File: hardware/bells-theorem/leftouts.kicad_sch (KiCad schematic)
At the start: 45 parts, among them U10 TL074, U8 TL074, U9 TL074

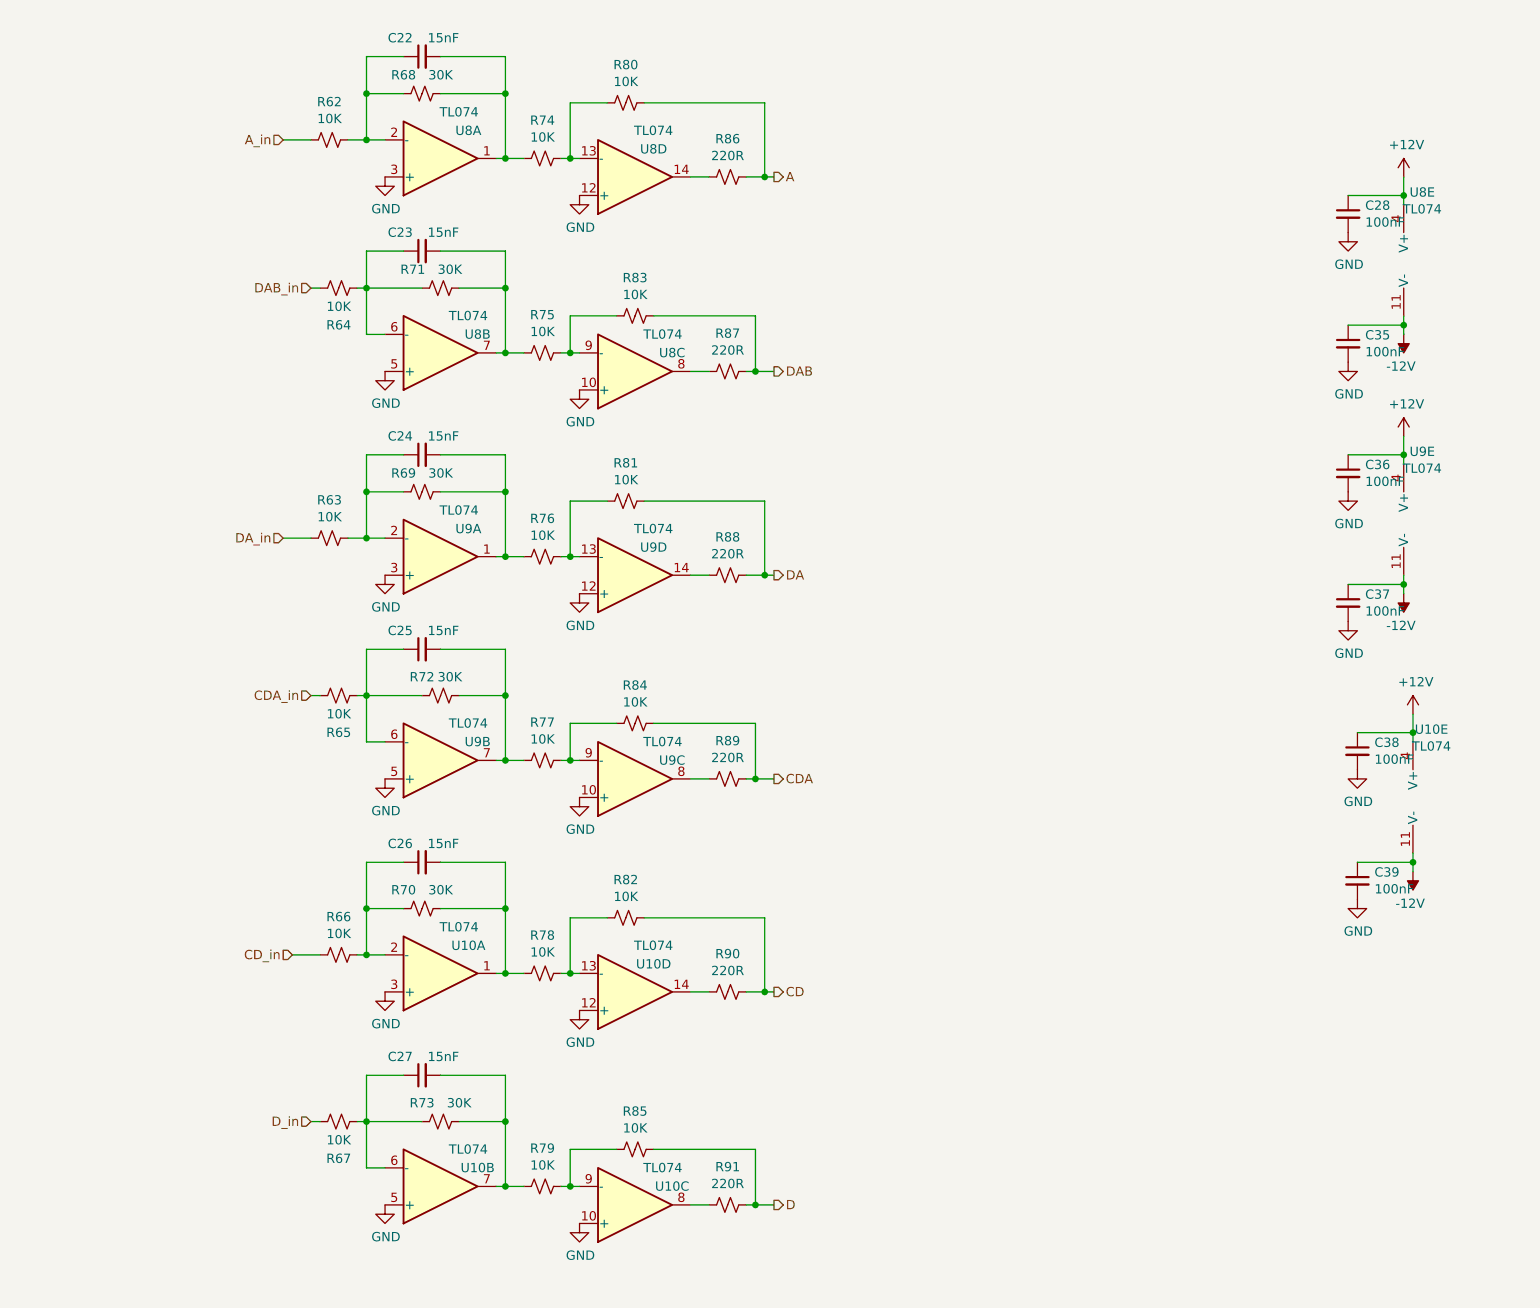
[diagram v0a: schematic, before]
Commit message: Modified with Jim M's recommendations for input scaling
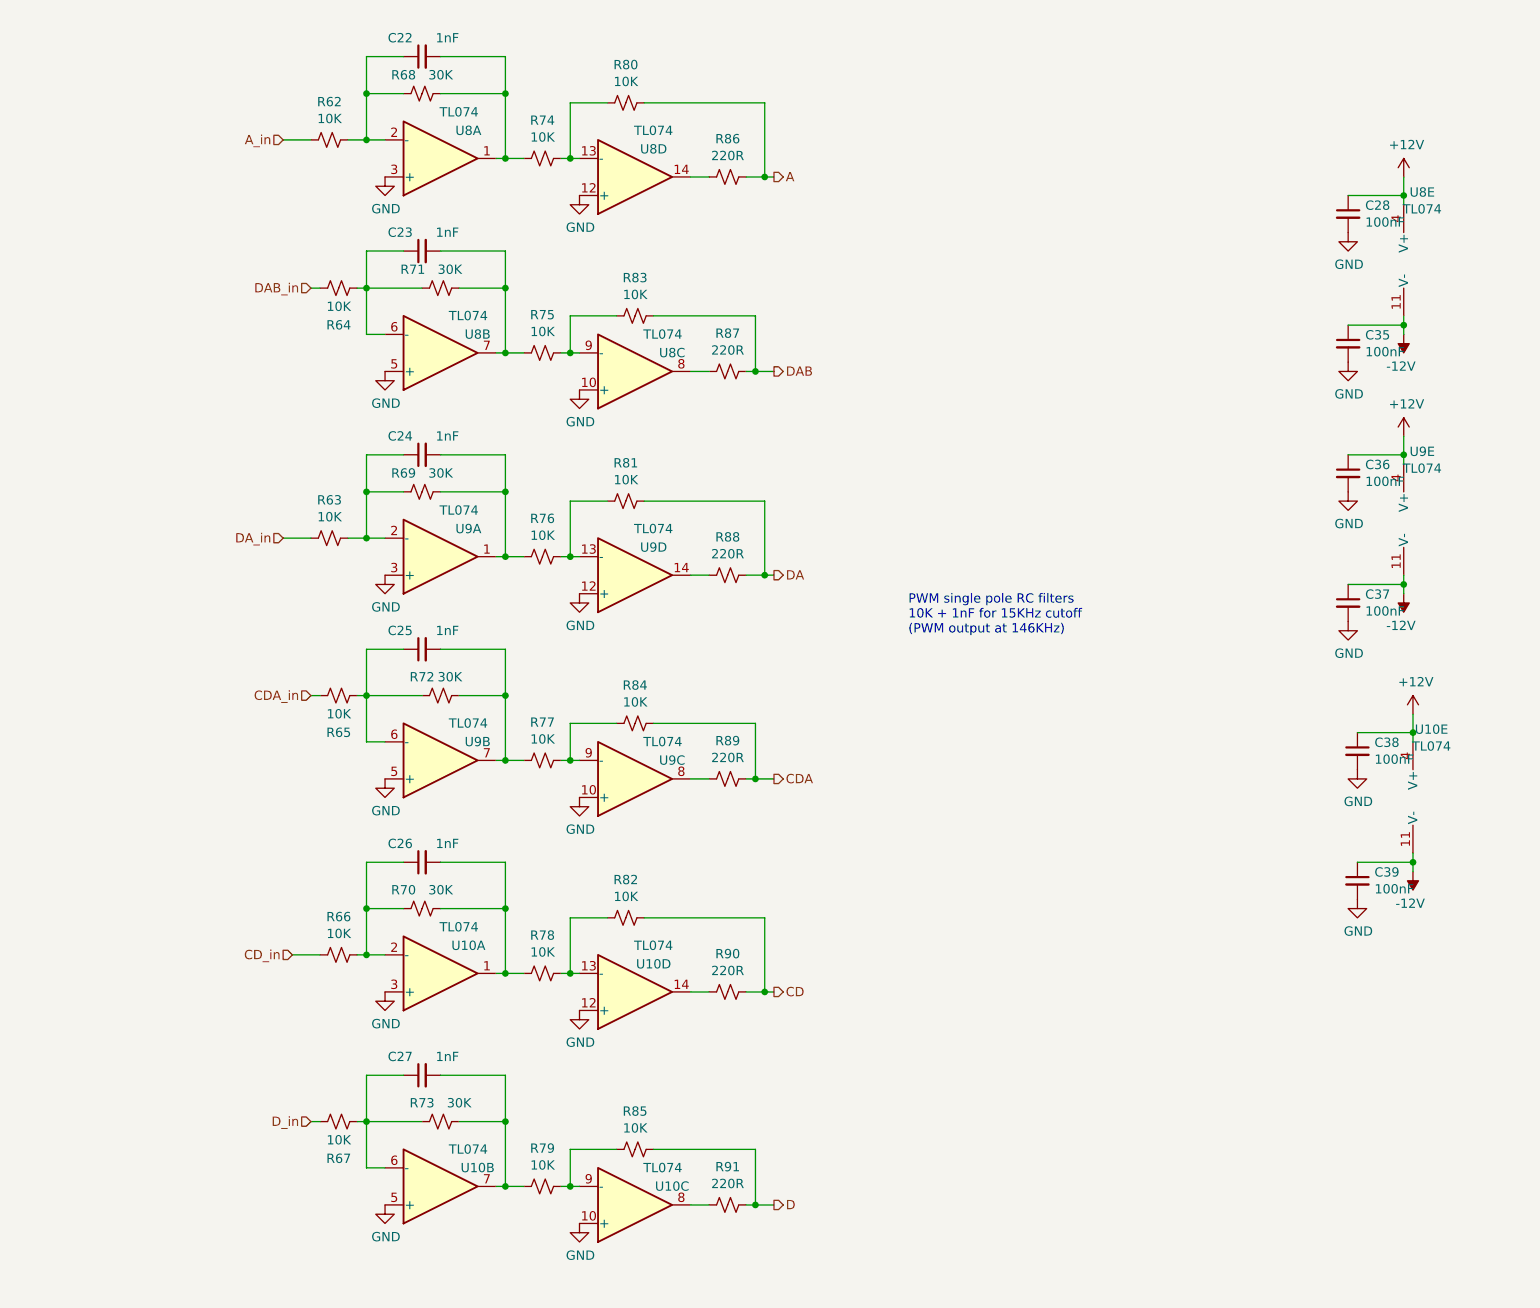
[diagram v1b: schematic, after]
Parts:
- C22, C23, C24, C25, C26, C27: value 15nF -> 1nF
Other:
- note added: "PWM single pole RC filters 10K + 1nF for 15KHz cutoff (PWM output at 146KHz)"
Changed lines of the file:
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@@
     (stroke (width 0) (type default) (color 0 0 0 0))
+  )
+  (text "PWM single pole RC filters\n10K + 1nF for 15KHz cutoff\n(PWM output at 146KHz)"
+    (at 142.875 99.695 0)
+    (effects (font (size 1.27 1.27)) (justify left bottom))
   )
   (hierarchical_label "CD_in" (shape input) (at 58.42 143.51 180)
@@
       (effects (font (size 1.27 1.27)) (justify left))
     )
-    (property "Value" "15nF" (id 1) (at 81.28 17.78 90)
+    (property "Value" "1nF" (id 1) (at 81.28 17.78 90)
       (effects (font (size 1.27 1.27)) (justify left))
     )
@@
       (effects (font (size 1.27 1.27)) (justify left))
     )
-    (property "Value" "15nF" (id 1) (at 81.28 44.45 90)
+    (property "Value" "1nF" (id 1) (at 81.28 44.45 90)
       (effects (font (size 1.27 1.27)) (justify left))
     )
@@
       (effects (font (size 1.27 1.27)) (justify left))
     )
-    (property "Value" "15nF" (id 1) (at 81.28 72.39 90)
+    (property "Value" "1nF" (id 1) (at 81.28 72.39 90)
       (effects (font (size 1.27 1.27)) (justify left))
     )
@@
       (effects (font (size 1.27 1.27)) (justify left))
     )
-    (property "Value" "15nF" (id 1) (at 81.28 99.06 90)
+    (property "Value" "1nF" (id 1) (at 81.28 99.06 90)
       (effects (font (size 1.27 1.27)) (justify left))
     )
@@
       (effects (font (size 1.27 1.27)) (justify left))
     )
-    (property "Value" "15nF" (id 1) (at 81.28 128.27 90)
+    (property "Value" "1nF" (id 1) (at 81.28 128.27 90)
       (effects (font (size 1.27 1.27)) (justify left))
     )
@@
       (effects (font (size 1.27 1.27)) (justify left))
     )
-    (property "Value" "15nF" (id 1) (at 81.28 157.48 90)
+    (property "Value" "1nF" (id 1) (at 81.28 157.48 90)
       (effects (font (size 1.27 1.27)) (justify left))
     )

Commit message: All changes up to date with latest revisions
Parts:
- C22, C23, C24, C25, C26, C27, C28, C35, C36, C37, C38, C39: footprint Capacitor_SMD:C_0805_2012Metric_Pad1.15x1.40mm_HandSolder -> Capacitor_SMD:C_0805_2012Metric_Pad1.18x1.45mm_HandSolder
- R62, R63, R64, R65, R66, R67, R68, R69, R70, R71, R72, R73, R74, R75, R76, R77, R78, R79, R80, R81, R82, R83, R84, R85, R86, R87, R88, R89, R90, R91: footprint Resistor_SMD:R_0805_2012Metric_Pad1.15x1.40mm_HandSolder -> Resistor_SMD:R_0805_2012Metric_Pad1.20x1.40mm_HandSolder
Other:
- title: (none) -> Bell's Theorem

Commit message: last hardware / software updates
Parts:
- removed C35, C37, C39: 100nF, Capacitor_SMD:C_0805_2012Metric_Pad1.18x1.45mm_HandSolder, symbol Device:C_Small
- added C34, C54, C55, C56, C57, C58: 2n, Capacitor_SMD:C_0805_2012Metric_Pad1.18x1.45mm_HandSolder, symbol Device:C_Small
- C22, C23, C24, C25, C26, C27: value 1nF -> 3.3n
- U10, U8, U9: symbol Amplifier_Operational:TL074 -> Amplifier_Operational:MCP6004
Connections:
- net -12V is gone; now on net GND: U10.11 (V-), U8.11 (V-), U9.11 (V-)
- net A: now also C34.2
- net CD: now also C54.2
- net CDA: now also C56.2
- net D: now also C58.2
- net DA: now also C55.2
- net DAB: now also C57.2
- net at R74.1, R80.2, U8.13 (-): now also C34.1
- net at R75.1, R83.2, U8.9 (-): now also C57.1
- net at R76.1, R81.2, U9.13 (-): now also C55.1
- net at R77.1, R84.2, U9.9 (-): now also C56.1
- net at R78.1, R82.2, U10.13 (-): now also C54.1
- net at R79.1, R85.2, U10.9 (-): now also C58.1
- net +12V renamed +10V
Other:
- note removed: "PWM single pole RC filters 10K + 1nF for 15KHz cutoff (PWM output at 146KHz)"

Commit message: version 0.6 hardware and code
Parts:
- added C15, C17, C5: 100nF, Capacitor_SMD:C_0805_2012Metric_Pad1.18x1.45mm_HandSolder, symbol Device:C_Small
- U10, U8, U9: value TL074 -> TLV9304; symbol Amplifier_Operational:MCP6004 -> Amplifier_Operational:TLC274
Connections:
- net GND: now also C15.2, C17.2, C5.2; no longer U10.11 (V-), U8.11 (V-), U9.11 (V-)
- new net -10V: C15.1, C17.1, C5.1, U10.11 (V-), U8.11 (V-), U9.11 (V-)
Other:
- note added: "TLC274/272 as previously thought doesn't technically support 24V diff supply"
- note added: "doing this architecture with single sided supplies is a lot more complicated than it might look. So using dual supply."
